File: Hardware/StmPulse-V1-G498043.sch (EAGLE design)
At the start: 59 parts, among them IC1 78M05, IC2 MCP6004D, T1_CLOCK 2N3904, T2_RESET TRANSISTOR_MMBT3904, U1 MCP6004D, U2-MCP4922 MCP4922MCP4922-SO14

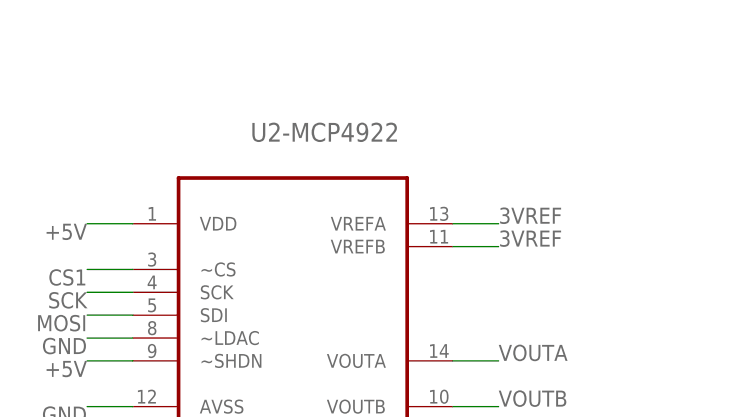
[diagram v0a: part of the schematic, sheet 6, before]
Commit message: updated BOM and RS component
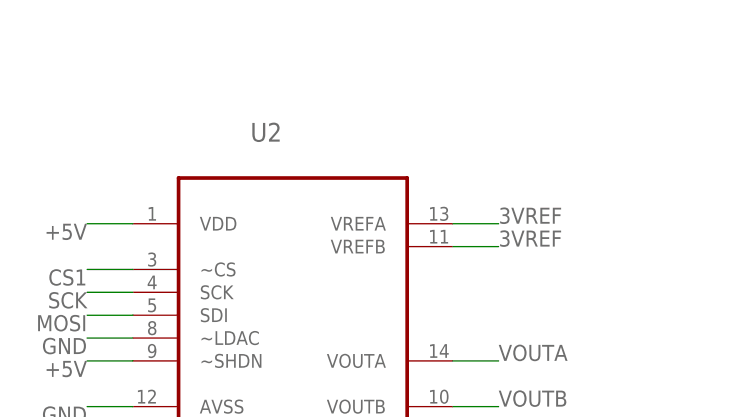
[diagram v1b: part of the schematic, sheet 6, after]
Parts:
- POWER: RS-PART (none) -> 828-1783
- renumbered U2-MCP4922 to U2
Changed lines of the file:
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@@
 <part name="C4" library="GMSN" deviceset="CAPACITOR_POL-US" device="153CLV-0505" value="10u"/>
 <part name="GND8" library="GMSN" deviceset="GND" device=""/>
-<part name="POWER" library="SparkFun-Connectors" library_urn="urn:adsk.eagle:library:513" deviceset="CONN_05X2" device="SHD_SMD" package3d_urn="urn:adsk.eagle:package:38003/1"/>
+<part name="POWER" library="SparkFun-Connectors" library_urn="urn:adsk.eagle:library:513" deviceset="CONN_05X2" device="SHD_SMD" package3d_urn="urn:adsk.eagle:package:38003/1">
+<attribute name="RS-PART" value="828-1783"/>
+</part>
 <part name="C7" library="GMSN" deviceset="CAPACITOR_POL-US" device="153CLV-0505" value="10u"/>
 <part name="IC1" library="GMSN" deviceset="VOLTAGE_REG_POS" device="DT" technology="05" value="78M05"/>
@@
 <part name="CV2" library="INSTRUO" deviceset="S_JACK" device="" value="S_JACK"/>
 <part name="C5" library="rcl" deviceset="C-US" device="C0805K" value="100n"/>
-<part name="U2-MCP4922" library="GMSN-R2Project" deviceset="MCP4922" device="MCP4922-SO14" value="MCP4922MCP4922-SO14">
+<part name="U2" library="GMSN-R2Project" deviceset="MCP4922" device="MCP4922-SO14" value="MCP4922MCP4922-SO14">
 <attribute name="RS-PART" value="402-910 "/>
 </part>
@@
 <attribute name="VALUE" x="33.02" y="63.5" size="1.778" layer="96" rot="R180"/>
 <attribute name="NAME" x="33.02" y="44.958" size="1.778" layer="95" rot="R180"/>
+<attribute name="RS-PART" x="30.48" y="53.34" size="1.778" layer="96" rot="R180" display="off"/>
 </instance>
 <instance part="C7" gate="G$1" x="111.76" y="60.96" smashed="yes">
@@
 <attribute name="VALUE" x="117.856" y="31.369" size="1.778" layer="96"/>
 </instance>
-<instance part="U2-MCP4922" gate="G$1" x="35.56" y="68.58" smashed="yes">
+<instance part="U2" gate="G$1" x="35.56" y="68.58" smashed="yes">
 <attribute name="RS-PART" x="35.56" y="68.58" size="1.778" layer="96" display="off"/>
 <attribute name="NAME" x="30.8356" y="87.8586" size="2.0828" layer="95" ratio="10" rot="SR0"/>
@@
 <net name="SCK" class="0">
 <segment>
-<pinref part="U2-MCP4922" gate="G$1" pin="SCK"/>
+<pinref part="U2" gate="G$1" pin="SCK"/>
 <wire x1="17.78" y1="71.12" x2="12.7" y2="71.12" width="0.1524" layer="91"/>
 <label x="12.7" y="71.12" size="1.778" layer="95" rot="R180"/>
@@
 <net name="MOSI" class="0">
 <segment>
-<pinref part="U2-MCP4922" gate="G$1" pin="SDI"/>
+<pinref part="U2" gate="G$1" pin="SDI"/>
 <wire x1="17.78" y1="68.58" x2="12.7" y2="68.58" width="0.1524" layer="91"/>
 <label x="12.7" y="68.58" size="1.778" layer="95" rot="R180"/>
@@
 </segment>
 <segment>
-<pinref part="U2-MCP4922" gate="G$1" pin="VOUTA"/>
+<pinref part="U2" gate="G$1" pin="VOUTA"/>
 <wire x1="53.34" y1="63.5" x2="58.42" y2="63.5" width="0.1524" layer="91"/>
 <label x="58.42" y="63.5" size="1.778" layer="95"/>
@@
 </segment>
 <segment>
-<pinref part="U2-MCP4922" gate="G$1" pin="VOUTB"/>
+<pinref part="U2" gate="G$1" pin="VOUTB"/>
 <wire x1="53.34" y1="58.42" x2="58.42" y2="58.42" width="0.1524" layer="91"/>
 <label x="58.42" y="58.42" size="1.778" layer="95"/>
@@
 </segment>
 <segment>
-<pinref part="U2-MCP4922" gate="G$1" pin="~LDAC"/>
+<pinref part="U2" gate="G$1" pin="~LDAC"/>
 <wire x1="17.78" y1="66.04" x2="12.7" y2="66.04" width="0.1524" layer="91"/>
 <label x="12.7" y="66.04" size="1.778" layer="95" rot="R180"/>
 </segment>
 <segment>
-<pinref part="U2-MCP4922" gate="G$1" pin="AVSS"/>
+<pinref part="U2" gate="G$1" pin="AVSS"/>
 <wire x1="17.78" y1="58.42" x2="12.7" y2="58.42" width="0.1524" layer="91"/>
 <label x="12.7" y="58.42" size="1.778" layer="95" rot="R180"/>
@@
 <net name="CS1" class="0">
 <segment>
-<pinref part="U2-MCP4922" gate="G$1" pin="~CS"/>
+<pinref part="U2" gate="G$1" pin="~CS"/>
 <wire x1="17.78" y1="73.66" x2="12.7" y2="73.66" width="0.1524" layer="91"/>
 <label x="12.7" y="73.66" size="1.778" layer="95" rot="R180"/>
@@
 <net name="3VREF" class="0">
 <segment>
-<pinref part="U2-MCP4922" gate="G$1" pin="VREFA"/>
+<pinref part="U2" gate="G$1" pin="VREFA"/>
 <wire x1="53.34" y1="78.74" x2="58.42" y2="78.74" width="0.1524" layer="91"/>
 <label x="58.42" y="78.74" size="1.778" layer="95"/>
 </segment>
 <segment>
-<pinref part="U2-MCP4922" gate="G$1" pin="VREFB"/>
+<pinref part="U2" gate="G$1" pin="VREFB"/>
 <wire x1="53.34" y1="76.2" x2="58.42" y2="76.2" width="0.1524" layer="91"/>
 <label x="58.42" y="76.2" size="1.778" layer="95"/>
@@
 </segment>
 <segment>
-<pinref part="U2-MCP4922" gate="G$1" pin="VDD"/>
+<pinref part="U2" gate="G$1" pin="VDD"/>
 <wire x1="17.78" y1="78.74" x2="12.7" y2="78.74" width="0.1524" layer="91"/>
 <label x="12.7" y="78.74" size="1.778" layer="95" rot="R180"/>
 </segment>
 <segment>
-<pinref part="U2-MCP4922" gate="G$1" pin="~SHDN"/>
+<pinref part="U2" gate="G$1" pin="~SHDN"/>
 <wire x1="17.78" y1="63.5" x2="12.7" y2="63.5" width="0.1524" layer="91"/>
 <label x="12.7" y="63.5" size="1.778" layer="95" rot="R180"/>
